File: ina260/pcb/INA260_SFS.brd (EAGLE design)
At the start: 85 x 56 mm, 65 parts

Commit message: Least check before order
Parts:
- moved POWERIN1 3.00 mm to (5.91, 33.8)
- moved PI4 1.00 mm to (71.5, 4.11)
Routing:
- net IN+: track 232.7 -> 233.6 mm
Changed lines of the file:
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@@
 <drawing>
 <settings>
-<setting alwaysvectorfont="yes"/>
+<setting alwaysvectorfont="no"/>
 <setting verticaltext="up"/>
 </settings>
@@
 <text x="35" y="6" size="1.016" layer="25">  OUT 1
 </text>
-<text x="65.5" y="7.7" size="1.016" layer="25">  OUT 4 </text>
+<text x="64" y="7.2" size="1.016" layer="25">  OUT 4 </text>
 <text x="14.6" y="44.4" size="1.016" layer="25">  OUT 2
 </text>
@@
 <attribute name="NAME" x="53.5" y="4.6" size="1.27" layer="25"/>
 </element>
-<element name="POWERIN1" library="Phoenix_connector_DJ" package="CON_3.81MM2" value="CON_3.81MM2_SIDE" x="5.91" y="36.75" smashed="yes" rot="R90">
-<attribute name="NAME" x="-3.05" y="34.54" size="1.27" layer="25" rot="R90"/>
+<element name="POWERIN1" library="Phoenix_connector_DJ" package="CON_3.81MM2" value="CON_3.81MM2_SIDE" x="5.91" y="33.75" smashed="yes" rot="R90">
+<attribute name="NAME" x="-3.05" y="31.54" size="1.27" layer="25" rot="R90"/>
 </element>
 <element name="PI1" library="Phoenix_connector_DJ" package="CON_3.81MM2" value="CON_3.81MM2_SIDE" x="40" y="4" smashed="yes" rot="R180">
 <attribute name="NAME" x="42.21" y="-4.96" size="1.27" layer="25" rot="R180"/>
 </element>
-<element name="PI4" library="Phoenix_connector_DJ" package="CON_3.81MM2" value="CON_3.81MM2_SIDE" x="70.55" y="4.11" smashed="yes" rot="R180">
-<attribute name="NAME" x="72.76" y="-4.85" size="1.27" layer="25" rot="R180"/>
+<element name="PI4" library="Phoenix_connector_DJ" package="CON_3.81MM2" value="CON_3.81MM2_SIDE" x="71.55" y="4.11" smashed="yes" rot="R180">
+<attribute name="NAME" x="73.76" y="-4.85" size="1.27" layer="25" rot="R180"/>
 </element>
 <element name="PI2" library="Phoenix_connector_DJ" package="CON_3.81MM2" value="CON_3.81MM2_SIDE" x="15.98" y="50.86" smashed="yes">
@@
 <element name="U$69" library="SFS" package="SOLDERJUMPER_ARROW_NOPASTE" value="JUMPER" x="46.7" y="11" smashed="yes" rot="R90"/>
 <element name="R1" library="rcl" library_urn="urn:adsk.eagle:library:334" package="M0805" package3d_urn="urn:adsk.eagle:package:23556/2" value="4K7" x="70.7" y="9.4" smashed="yes" rot="R270">
-<attribute name="NAME" x="72.13" y="9.07" size="1.27" layer="25"/>
+<attribute name="NAME" x="69.63" y="12.07" size="1.27" layer="25"/>
 <attribute name="POPULARITY" value="45" x="70.7" y="9.4" size="1.778" layer="27" rot="R270" display="off"/>
 <attribute name="SPICEPREFIX" value="R" x="70.7" y="9.4" size="1.778" layer="27" rot="R270" display="off"/>
@@
 <contactref element="BUS1" pad="P$2"/>
 <wire x1="60" y1="24.05" x2="60" y2="28.1" width="0.3" layer="1"/>
-<wire x1="70.7" y1="10.35" x2="70.525" y2="10.525" width="0.3" layer="1"/>
 <wire x1="78" y1="9.19" x2="76.31" y2="9.19" width="0.3" layer="1"/>
-<wire x1="76.31" y1="9.19" x2="74.975" y2="10.525" width="0.3" layer="1"/>
+<wire x1="74.975" y1="10.525" x2="76.31" y2="9.19" width="0.3" layer="1"/>
+<wire x1="70.7" y1="13.35" x2="60" y2="24.05" width="0.3" layer="1"/>
+<wire x1="70.7" y1="10.35" x2="70.7" y2="13.35" width="0.3" layer="1"/>
 <wire x1="70.7" y1="10.35" x2="70.875" y2="10.525" width="0.3" layer="1"/>
 <wire x1="70.875" y1="10.525" x2="74.975" y2="10.525" width="0.3" layer="1"/>
-<wire x1="70.7" y1="10.35" x2="70.5" y2="10.55" width="0.3" layer="1"/>
-<wire x1="70.5" y1="13.55" x2="60" y2="24.05" width="0.3" layer="1"/>
-<wire x1="70.5" y1="10.55" x2="70.5" y2="13.55" width="0.3" layer="1"/>
 </signal>
 <signal name="SCL">
@@
 <wire x1="23.775" y1="37.75" x2="23.725" y2="37.75" width="3" layer="1"/>
 <wire x1="22.375" y1="36.35" x2="13" y2="36.35" width="3" layer="1"/>
-<wire x1="6.31" y1="36.35" x2="13" y2="36.35" width="3" layer="1"/>
-<wire x1="6.31" y1="36.35" x2="5.91" y2="36.75" width="3" layer="1"/>
+<wire x1="8.51" y1="36.35" x2="13" y2="36.35" width="3" layer="1"/>
+<wire x1="8.51" y1="36.35" x2="5.91" y2="33.75" width="3" layer="1"/>
 <wire x1="22.375" y1="36.35" x2="24.525" y2="38.5" width="3" layer="1"/>
 <wire x1="47.37" y1="34.43" x2="43.45" y2="30.51" width="3" layer="1"/>
@@
 <contactref element="U$16" pad="P16"/>
 <contactref element="PI4" pad="P$2"/>
-<wire x1="66.74" y1="6.11" x2="66.74" y2="4.11" width="3" layer="1"/>
-<wire x1="66.74" y1="6.11" x2="63.85" y2="9" width="3" layer="1"/>
+<wire x1="67.74" y1="5.11" x2="67.74" y2="4.11" width="3" layer="1"/>
+<wire x1="67.74" y1="5.11" x2="63.85" y2="9" width="3" layer="1"/>
 <wire x1="59.65" y1="9" x2="58.55" y2="10.1" width="3" layer="1"/>
 <wire x1="63.85" y1="9" x2="59.65" y2="9" width="3" layer="1"/>

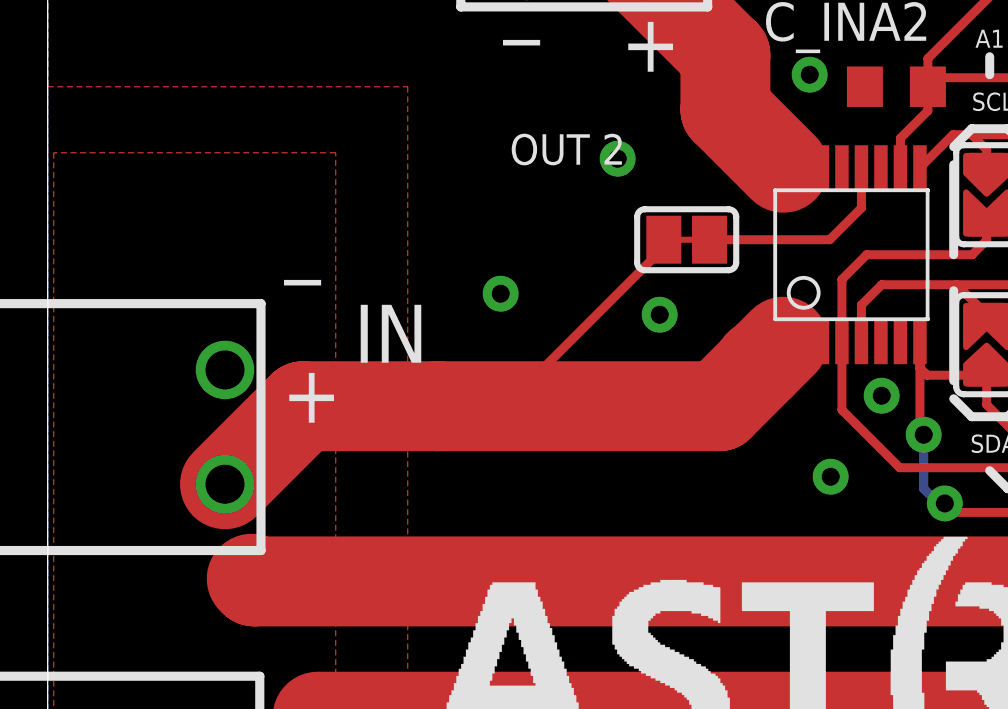
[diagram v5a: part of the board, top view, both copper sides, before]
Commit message: misplaced names corectted on this version
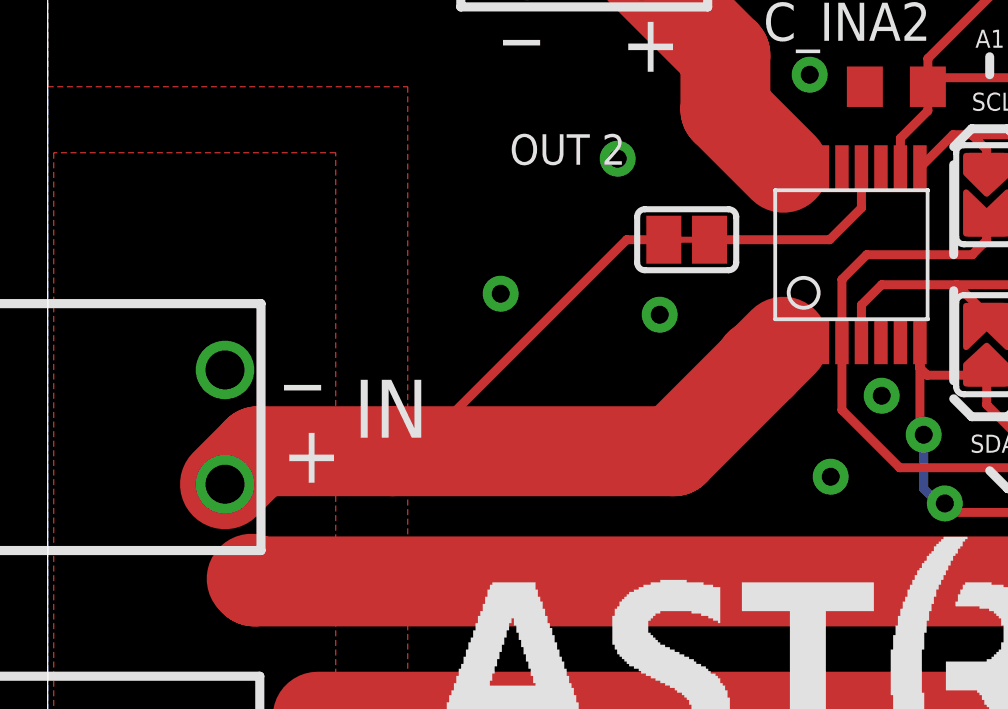
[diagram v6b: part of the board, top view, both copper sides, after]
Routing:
- net IN+: track 233.6 -> 235.6 mm
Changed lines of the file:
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@@
 <drawing>
 <settings>
-<setting alwaysvectorfont="no"/>
+<setting alwaysvectorfont="yes"/>
 <setting verticaltext="up"/>
 </settings>
@@
 <text x="39.3" y="6.6" size="1.9304" layer="25">_</text>
 <text x="69.9" y="6.7" size="1.9304" layer="25">_</text>
-<text x="7.9" y="41" size="1.9304" layer="25">_</text>
+<text x="7.9" y="37.5" size="1.9304" layer="25">_</text>
 <text x="7.9" y="25.7" size="1.9304" layer="25">_</text>
-<text x="7.8" y="35.8" size="1.9304" layer="25">+</text>
+<text x="7.8" y="33.8" size="1.9304" layer="25">+</text>
 <text x="7.7" y="20.2" size="1.9304" layer="25">+</text>
-<text x="10.2" y="37.8" size="1.9304" layer="25">IN</text>
+<text x="10.2" y="35.3" size="1.9304" layer="25">IN</text>
 <text x="9.5" y="22.5" size="1.9304" layer="25">OUT</text>
 <text x="6.2" y="0.7" size="1.4224" layer="25">MAX 15A PER INA260</text>
@@
 <contactref element="POWERIN1" pad="P$1"/>
 <wire x1="23.775" y1="37.75" x2="23.725" y2="37.75" width="3" layer="1"/>
-<wire x1="22.375" y1="36.35" x2="13" y2="36.35" width="3" layer="1"/>
-<wire x1="8.51" y1="36.35" x2="13" y2="36.35" width="3" layer="1"/>
-<wire x1="8.51" y1="36.35" x2="5.91" y2="33.75" width="3" layer="1"/>
-<wire x1="22.375" y1="36.35" x2="24.525" y2="38.5" width="3" layer="1"/>
+<wire x1="20.875" y1="34.85" x2="11.5" y2="34.85" width="3" layer="1"/>
+<wire x1="7.01" y1="34.85" x2="11.5" y2="34.85" width="3" layer="1"/>
+<wire x1="7.01" y1="34.85" x2="5.91" y2="33.75" width="3" layer="1"/>
+<wire x1="20.875" y1="34.85" x2="24.525" y2="38.5" width="3" layer="1"/>
 <wire x1="47.37" y1="34.43" x2="43.45" y2="30.51" width="3" layer="1"/>
-<wire x1="20.538" y1="41.9" x2="20.538" y2="41.638" width="0.3" layer="1"/>
-<wire x1="20.538" y1="41.638" x2="15.9" y2="37" width="0.3" layer="1"/>
+<wire x1="20.538" y1="41.9" x2="19.3" y2="41.9" width="0.3" layer="1"/>
+<wire x1="19.3" y1="41.9" x2="12.25" y2="34.85" width="0.3" layer="1"/>
 <wire x1="25.825" y1="38.5" x2="25.175" y2="38.5" width="0.3" layer="1"/>
 <wire x1="25.175" y1="38.5" x2="24.525" y2="38.5" width="0.3" layer="1"/>
@@
 <vertex x="0.2" y="11.6"/>
 </polygon>
-<wire x1="13.65" y1="37" x2="13" y2="36.35" width="0.3" layer="1"/>
-<wire x1="15.9" y1="37" x2="13.65" y2="37" width="0.3" layer="1"/>
+<wire x1="12.25" y1="34.85" x2="11.5" y2="34.85" width="0.3" layer="1"/>
 <wire x1="47.37" y1="34.43" x2="46.038" y2="35.762" width="0.3" layer="1"/>
 <wire x1="46.038" y1="35.762" x2="46.038" y2="41.4" width="0.3" layer="1"/>

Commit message: ZIP file for jlc order
the zip file that was used to order the pcb's if new ones are needed this file can be used
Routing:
- net GND: vias 48 -> 49
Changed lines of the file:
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@@
 <?xml version="1.0" encoding="utf-8"?>
 <!DOCTYPE eagle SYSTEM "eagle.dtd">
-<eagle version="9.4.2">
+<eagle version="9.5.0">
 <drawing>
 <settings>
@@
 </polygon>
 <via x="19" y="44.6" extent="1-16" drill="0.6"/>
+<via x="13.6" y="42.6" extent="1-16" drill="0.6"/>
 </signal>
 <signal name="N$1">
@@
 <wire x1="78.578" y1="40.5" x2="75.95" y2="40.5" width="0.3" layer="1"/>
 </signal>
+<signal name="GND1">
+<via x="9.1" y="50.1" extent="1-16" drill="0.6"/>
+</signal>
+<signal name="GND2">
+<via x="66.1" y="51.6" extent="1-16" drill="0.6"/>
+</signal>
+<signal name="GND3">
+<via x="40.6" y="10.6" extent="1-16" drill="0.6"/>
+</signal>
+<signal name="GND4">
+<via x="46.1" y="3.6" extent="1-16" drill="0.6"/>
+</signal>
+<signal name="GND5">
+<via x="28.6" y="53.1" extent="1-16" drill="0.6"/>
+</signal>
+<signal name="GND6">
+<via x="56.6" y="53.1" extent="1-16" drill="0.6"/>
+</signal>
 </signals>

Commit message: update PCB silkscreen
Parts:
- added U$15: (no value), ed:ED_KLEIN
- moved U$10 22.3 mm to (14.5, 22.5)
- moved U$13 11.9 mm to (9.00, 11.7), turned to 90 degrees
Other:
- board text added: "Amsterdam University of Applied Sciences"
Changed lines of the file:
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@@
 <?xml version="1.0" encoding="utf-8"?>
 <!DOCTYPE eagle SYSTEM "eagle.dtd">
-<eagle version="9.5.0">
+<eagle version="9.4.2">
 <drawing>
 <settings>
@@
 <text x="6.2" y="0.7" size="1.4224" layer="25">MAX 15A PER INA260</text>
 <text x="69.5" y="42" size="1.27" layer="25">Power Monitoring</text>
-<text x="8" y="6.2" size="1.27" layer="25">HvA</text>
+<text x="15" y="24.7" size="1.27" layer="25">HvA</text>
 <text x="65.7" y="53.2" size="1.27" layer="26" rot="MR180">Made by:
 Maurizio Giannattasio
@@
 <text x="73.4" y="8.4" size="1.016" layer="25">SDA</text>
 <text x="73.9" y="12.7" size="1.016" layer="25">SCL</text>
+<text x="25" y="25.5" size="2.5" layer="21">           Amsterdam
+University of Applied Sciences</text>
 </plain>
 <attributes>
@@
 <element name="U$8" library="logos" package="JUMPER_INFO" value="" x="65.8" y="36.6" smashed="yes" rot="R180"/>
 <element name="U$9" library="logos" package="JUMPER_INFO" value="" x="39.8" y="36.6" smashed="yes" rot="R180"/>
-<element name="U$10" library="logos" package="HVA_LOGO" value="" x="0" y="5.5" smashed="yes"/>
-<element name="U$13" library="logos" package="ASTRON_LOGO" value="" x="12.7" y="23" smashed="yes"/>
+<element name="U$10" library="logos" package="HVA_LOGO" value="" x="14.5" y="22.5" smashed="yes"/>
+<element name="U$13" library="logos" package="ASTRON_LOGO" value="" x="9" y="11.7" smashed="yes" rot="R90"/>
 <element name="5V_ALIVE_LED" library="led" library_urn="urn:adsk.eagle:library:259" package="1206" package3d_urn="urn:adsk.eagle:package:15796/1" value="" x="80" y="40.5" smashed="yes">
 <attribute name="VALUE" x="78.73" y="37.96" size="1.27" layer="27"/>
@@
 <attribute name="NAME" x="86.96" y="15.21" size="1.27" layer="25" rot="R270"/>
 </element>
+<element name="U$15" library="ed" package="ED_KLEIN" value="" x="71.5" y="7" smashed="yes" rot="MR0"/>
 </elements>
 <signals>
